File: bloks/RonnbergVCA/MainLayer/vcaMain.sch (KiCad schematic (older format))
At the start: 32 parts, among them J1 Conn_02x03_Odd_Even, J10 Conn_02x03_Odd_Even, J11 Conn_02x03_Odd_Even, J12 Conn_02x03_Odd_Even, J1M1 Conn_01x01, J2 Conn_02x03_Odd_Even, J2M1 Conn_01x01, J3 Conn_02x03_Odd_Even, J3M1 Conn_01x01, J4 Conn_02x03_Odd_Even, J4M1 Conn_01x01, J5 Conn_02x03_Odd_Even, J5M1 Conn_01x01, J6 Conn_02x03_Odd_Even, J6M1 Conn_01x01, J7 Conn_02x03_Odd_Even, J7M1 Conn_01x01, J8 Conn_02x03_Odd_Even, J9 Conn_02x03_Odd_Even, U1 TL072, U2 CA3080

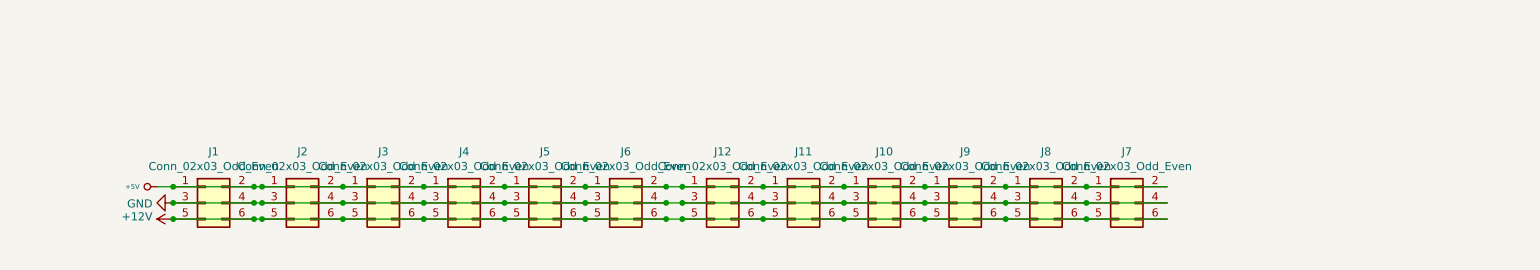
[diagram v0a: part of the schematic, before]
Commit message: Added -12v rail to power headers
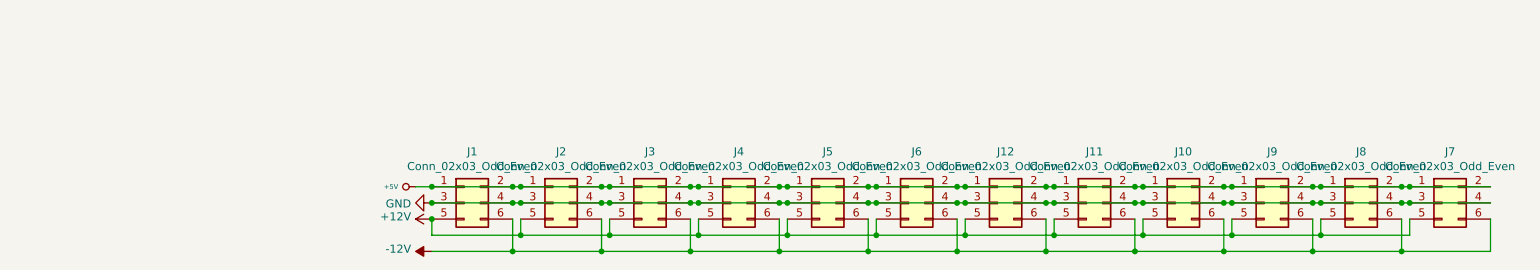
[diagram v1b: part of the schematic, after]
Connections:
- net +12V: no longer J1.6 (Pin_6), J10.6 (Pin_6), J11.6 (Pin_6), J12.6 (Pin_6), J2.6 (Pin_6), J3.6 (Pin_6), J4.6 (Pin_6), J5.6 (Pin_6), J6.6 (Pin_6), J7.6 (Pin_6), J8.6 (Pin_6), J9.6 (Pin_6)
- new net -12V: J1.6 (Pin_6), J10.6 (Pin_6), J11.6 (Pin_6), J12.6 (Pin_6), J2.6 (Pin_6), J3.6 (Pin_6), J4.6 (Pin_6), J5.6 (Pin_6), J6.6 (Pin_6), J7.6 (Pin_6), J8.6 (Pin_6), J9.6 (Pin_6)
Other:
- moved on the sheet: J1, J10, J11, J12, J2, J3, J4, J5, J6, J7, J8, J9
